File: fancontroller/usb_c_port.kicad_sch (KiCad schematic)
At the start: 13 parts, among them P2 USB_C_Plug, Q13 PNP, Q14 NPN, U1 CH340C, Y1 12Mhz

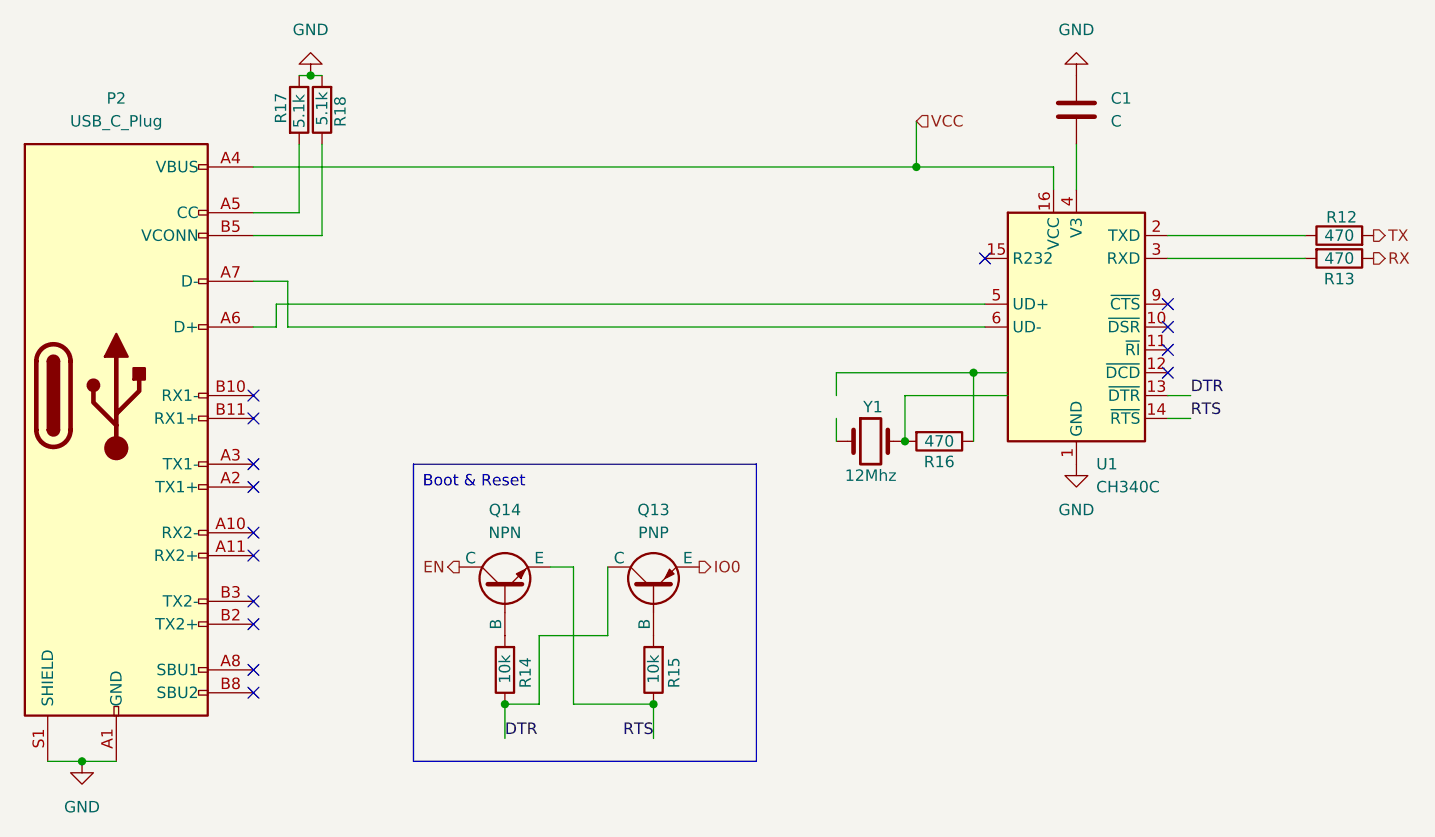
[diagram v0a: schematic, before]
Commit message: Restructure Fan drivers into separate modules and rework USB-C
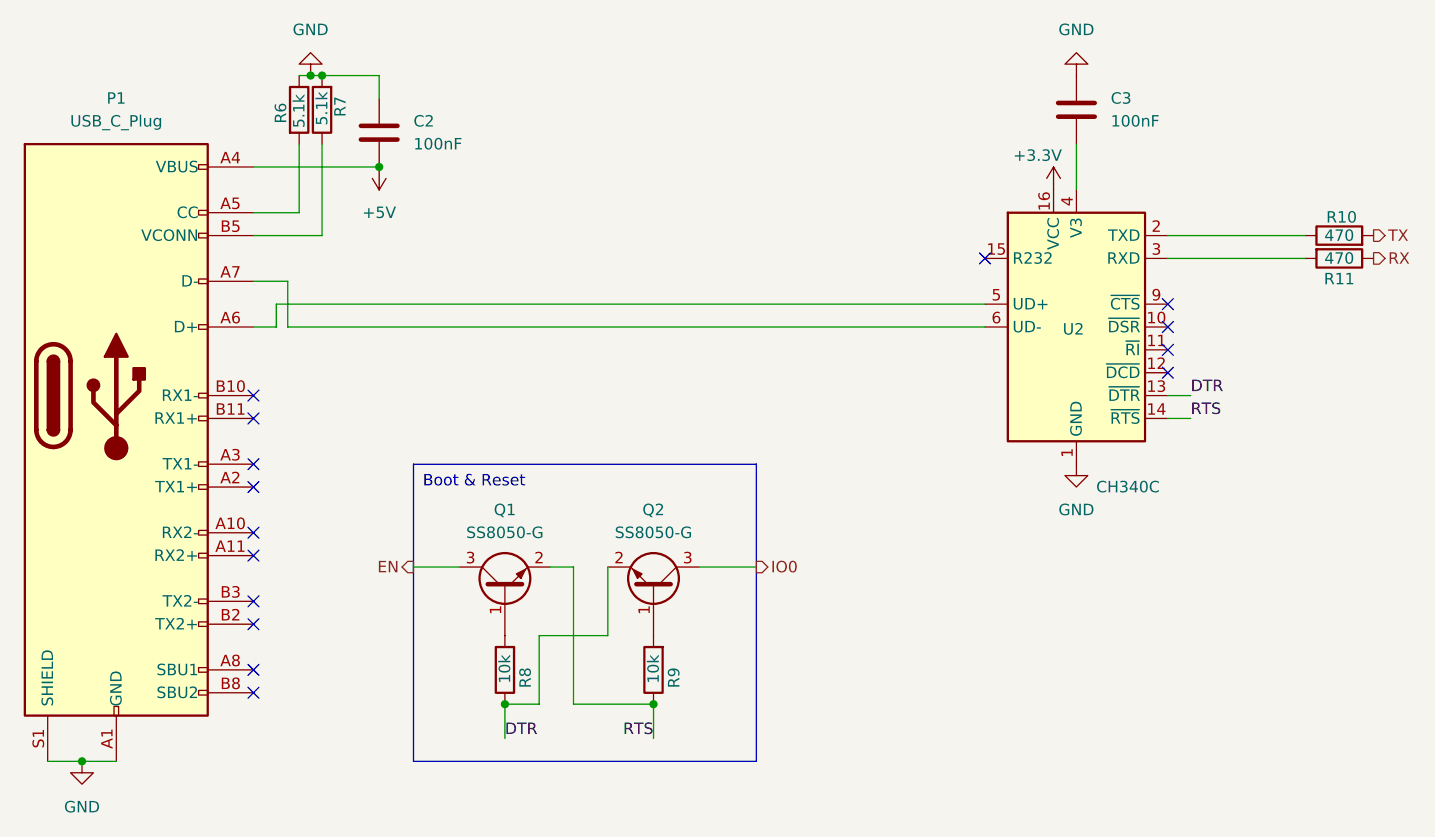
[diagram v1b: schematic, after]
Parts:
- removed Q13: PNP, symbol Simulation_SPICE:PNP
- removed Q14: NPN, symbol Simulation_SPICE:NPN
- removed R16: 470, symbol Device:R
- removed Y1: 12Mhz, symbol Device:Crystal
- added C2: 100nF, Capacitor_SMD:C_0805_2012Metric, symbol Device:C
- added Q1, Q2: SS8050-G, Package_TO_SOT_SMD:SOT-23, symbol Transistor_BJT:BC817
- C3: renamed from C1; value C -> 100nF; footprint (none) -> Capacitor_SMD:C_0805_2012Metric; LCSC Part # (none) -> C1525
- P1: renamed from P2; LCSC Part # (none) -> C456012
- R10: renamed from R12; footprint (none) -> Resistor_SMD:R_0805_2012Metric; LCSC Part # (none) -> C17710
- R11: renamed from R13; footprint (none) -> Resistor_SMD:R_0805_2012Metric; LCSC Part # (none) -> C17710
- R6: renamed from R17; footprint (none) -> Resistor_SMD:R_0805_2012Metric; LCSC Part # (none) -> C27834
- R7: renamed from R18; footprint (none) -> Resistor_SMD:R_0805_2012Metric; LCSC Part # (none) -> C27834
- R8: renamed from R14; footprint (none) -> Resistor_SMD:R_0805_2012Metric
- R9: renamed from R15; footprint (none) -> Resistor_SMD:R_0805_2012Metric
- U2: renamed from U1; LCSC Part # (none) -> C84681
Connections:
- net DTR: now also Q2.2 (E)
- net EN: now also Q1.3 (C)
- net GND: now also C2.1
- net IO0: now also Q2.3 (C)
- net RTS: now also Q1.2 (E)
- net at R9.2: now also Q2.1 (B)
- net at R8.2: now also Q1.1 (B)
- net VCC renamed +5V
- net +5V: now also C2.2; no longer U2.16 (VCC)
- new net +3.3V: U2.16 (VCC)

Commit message: Improve footprints and do massive overhaul for part numbering for better future order
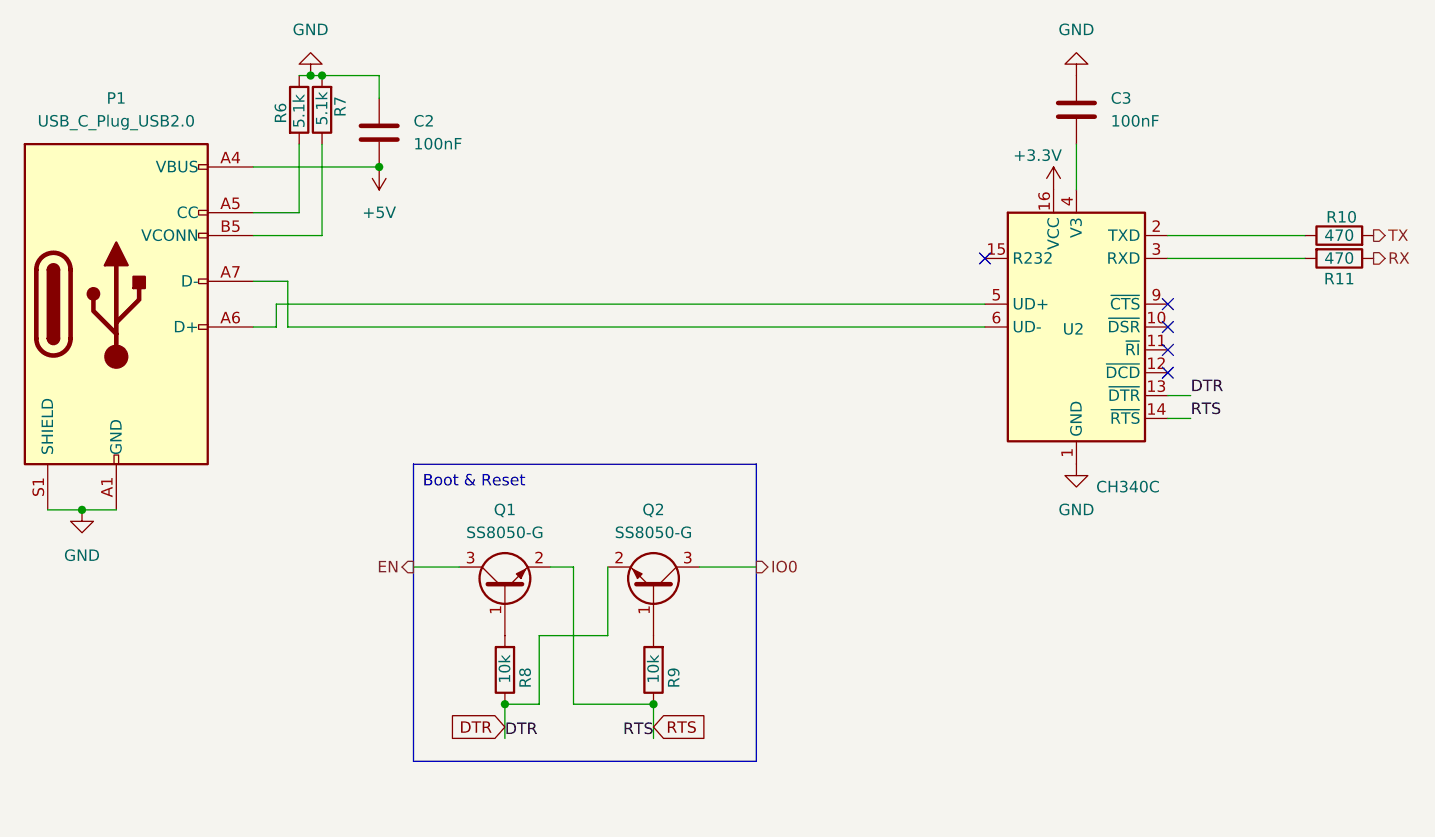
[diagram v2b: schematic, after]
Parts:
- removed P1: USB_C_Plug, symbol Connector:USB_C_Plug
- added P1: USB_C_Plug_USB2.0, Connector_USB:USB_C_Receptacle_HCTL_HC-TYPE-C-16P-01A, symbol Connector:USB_C_Plug_USB2.0
- R8, R9: LCSC Part # (none) -> C17414
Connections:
- net +5V: now also P1.A4 (VBUS), P1.A9 (VBUS), P1.B4 (VBUS), P1.B9 (VBUS)
- net GND: now also P1.A1 (GND), P1.A12 (GND), P1.B1 (GND), P1.B12 (GND), P1.S1 (SHIELD)
- net at U2.5 (UD+): now also P1.A6 (D+)
- net at U2.6 (UD-): now also P1.A7 (D-)
- net at R6.2: now also P1.A5 (CC)
- net at R7.1: now also P1.B5 (VCONN)
- no-connect marks 15 -> 5
